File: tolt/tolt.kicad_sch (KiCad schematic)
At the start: 9 parts, among them J2 USB_C_Receptacle_USB2.0

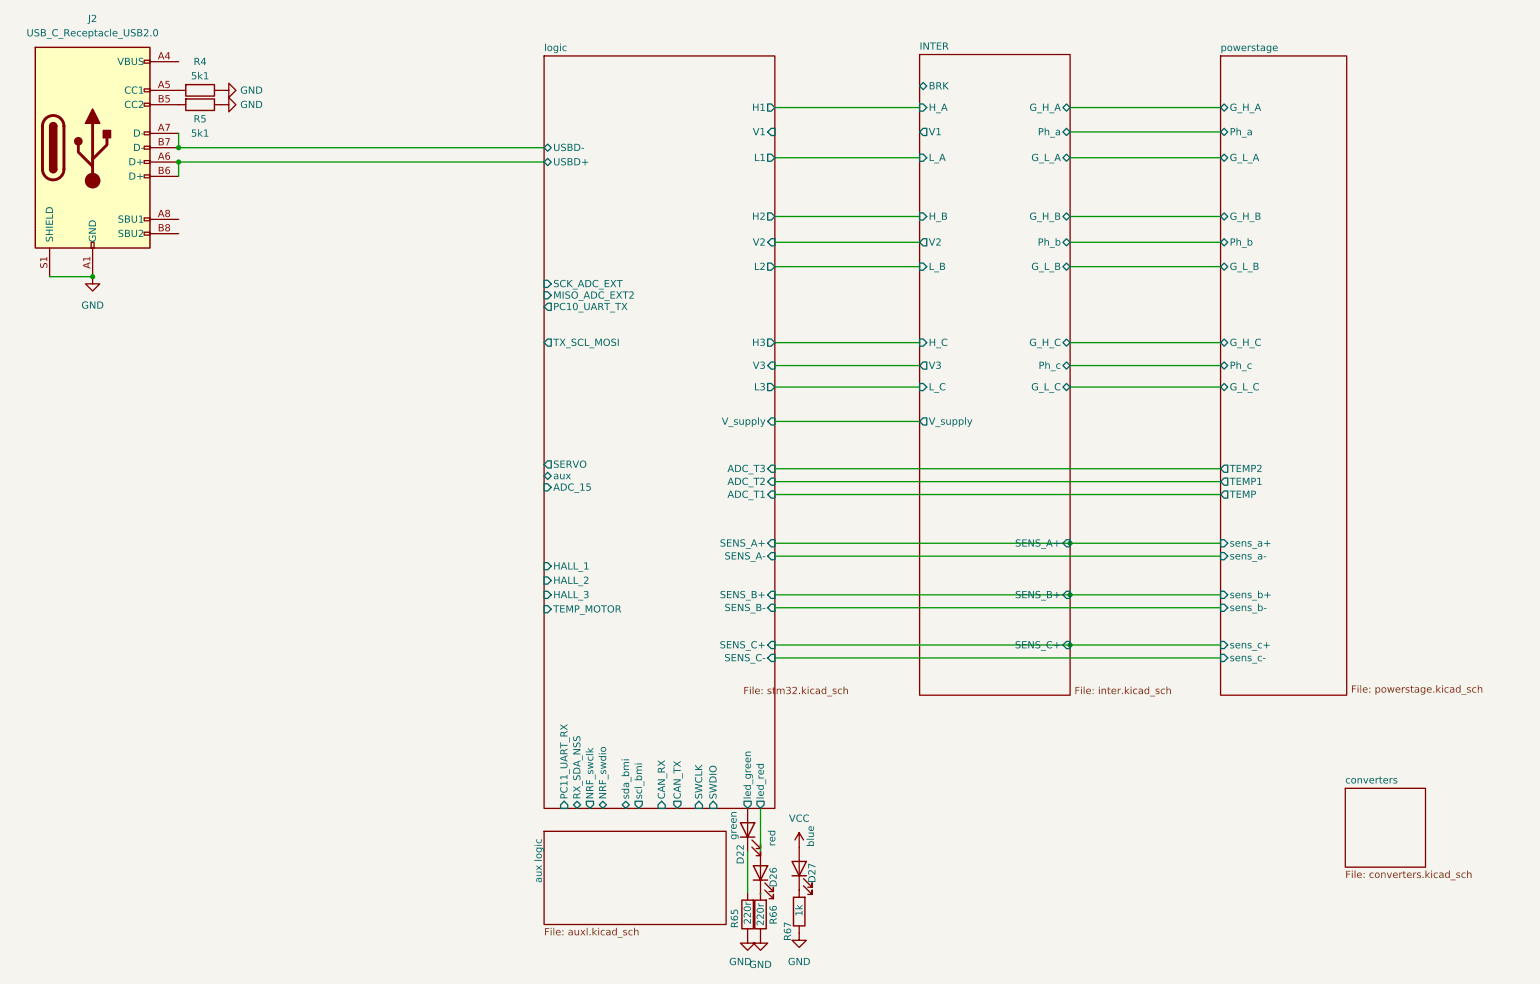
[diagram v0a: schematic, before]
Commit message: modified:   tolt/auxl.kicad_sch 	modified:   tolt/converters.kicad_sch 	modified:   tolt/powerstage.kicad_sch 	modified:   tolt/stm32.kicad_sch 	modified:   tolt/tolt.kicad_pcb 	modified:   tolt/tolt.kicad_pro 	modified:   tolt/tolt.kicad_sch 	SOP120P1500X235-17N.step 	tolt/Library.pretty/HDSOP-16-2.kicad_mod 	tolt/Library.pretty/R5930.kicad_mod 	tolt/conn.kicad_sch
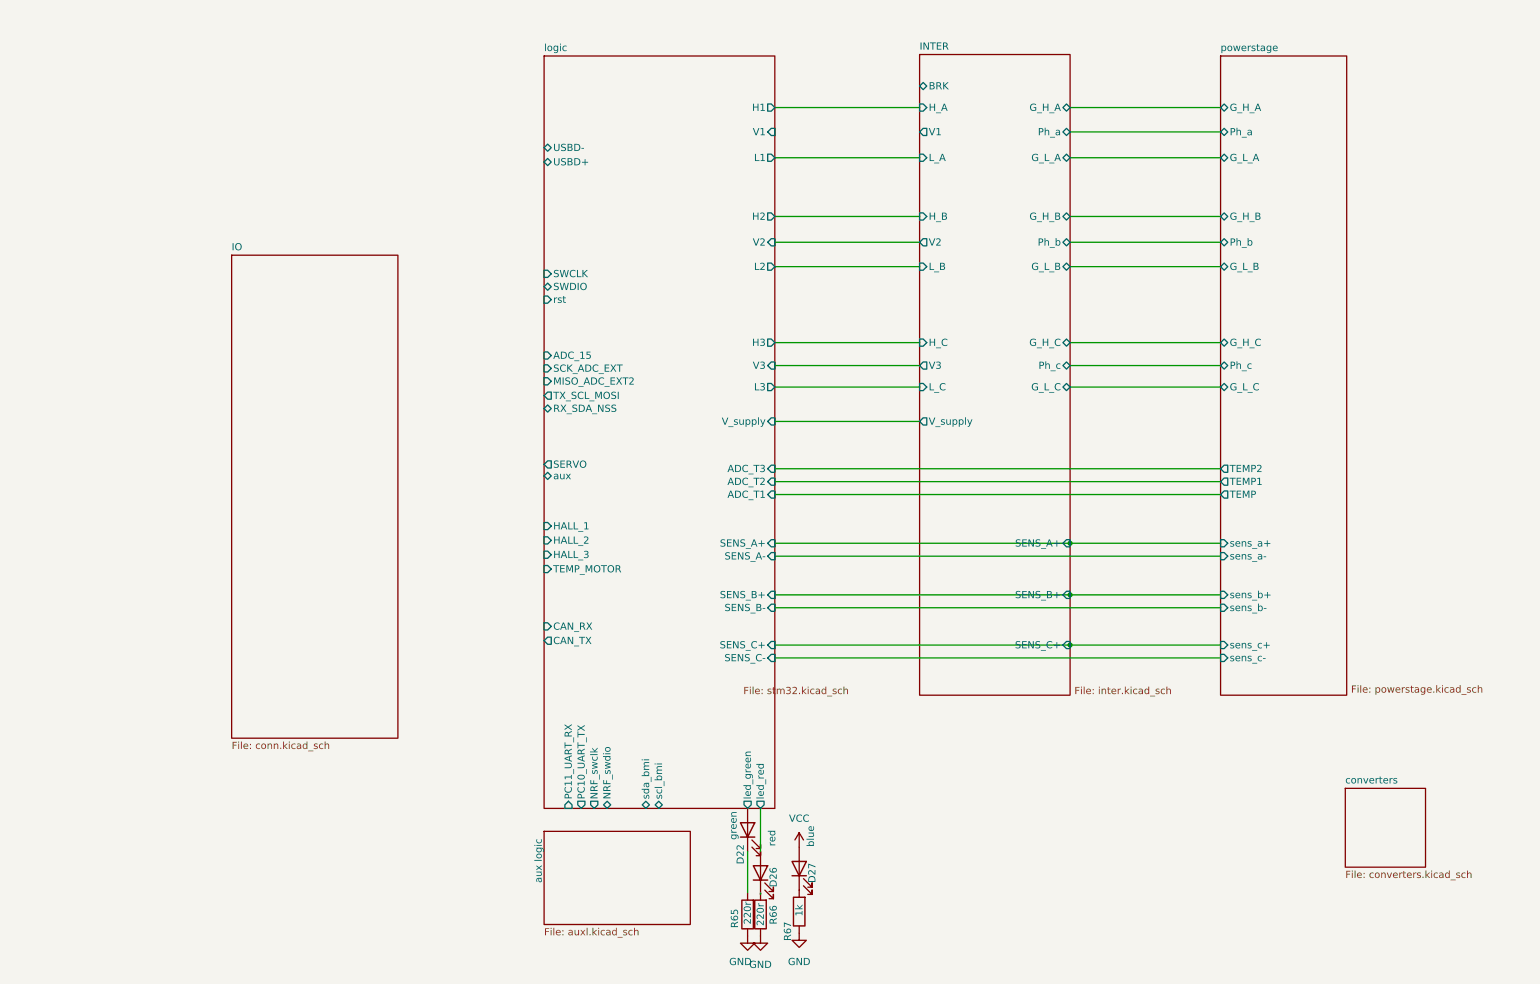
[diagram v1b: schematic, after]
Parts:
- removed J2: USB_C_Receptacle_USB2.0, Connector_USB:USB_C_Receptacle_G-Switch_GT-USB-7051x, symbol Connector:USB_C_Receptacle_USB2.0
- removed R4, R5: 5k1, Resistor_SMD:R_0603_1608Metric, symbol Device:R
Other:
- added sheet IO (conn.kicad_sch)
- sheet logic ports: added rst; removed none

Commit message: new file:   tolt/Library.pretty/IND-SMD_L3.9-W3.9-1.kicad_mod 	new file:   tolt/Library.pretty/IND-SMD_L5.0-W5.0.kicad_mod 	modified:   tolt/auxl.kicad_sch 	modified:   tolt/conn.kicad_sch 	modified:   tolt/converters.kicad_sch 	new file:   tolt/fp-lib-table 	modified:   tolt/inter.kicad_sch 	modified:   tolt/powerstage.kicad_sch 	modified:   tolt/stm32.kicad_sch 	modified:   tolt/tolt.kicad_sch
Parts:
- D22, D26, D27: footprint (none) -> Diode_SMD:D_0603_1608Metric_Pad1.05x0.95mm_HandSolder
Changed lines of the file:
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@@
 			)
 		)
-		(property "Footprint" ""
+		(property "Footprint" "Diode_SMD:D_0603_1608Metric_Pad1.05x0.95mm_HandSolder"
 			(at 146.812 165.354 0)
 			(effects
@@
 			)
 		)
-		(property "Footprint" ""
+		(property "Footprint" "Diode_SMD:D_0603_1608Metric_Pad1.05x0.95mm_HandSolder"
 			(at 153.67 164.592 0)
 			(effects
@@
 			)
 		)
-		(property "Footprint" ""
+		(property "Footprint" "Diode_SMD:D_0603_1608Metric_Pad1.05x0.95mm_HandSolder"
 			(at 144.526 157.734 0)
 			(effects
@@
 		)
 		(property "Sheetfile" "stm32.kicad_sch"
-			(at 143.764 132.334 0)
+			(at 153.67 150.876 0)
 			(effects
 				(font
@@
 	)
 	(sheet
-		(at 53.086 55.88)
-		(size 29.464 85.598)
+		(at 66.294 27.686)
+		(size 29.464 108.204)
 		(exclude_from_sim no)
 		(in_bom yes)
@@
 		)
 		(property "Sheetname" "IO"
-			(at 53.086 55.1684 0)
+			(at 66.294 26.9744 0)
 			(effects
 				(font
@@
 		)
 		(property "Sheetfile" "conn.kicad_sch"
-			(at 53.086 142.0626 0)
-			(effects
-				(font
+			(at 66.294 136.4746 0)
+			(effects
+				(font

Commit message: modified:   tolt/converters.kicad_sch 	modified:   tolt/inter.kicad_sch 	modified:   tolt/tolt.kicad_sch
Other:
- sheet IO ports: added ADC_15, CAN_RX, CAN_TX, HALL_1, HALL_2, HALL_3, MISO_ADC_EXT2, RX_SDA_NSS, SCK_ADC_EXT, SWCLK, SWDIO, TEMP_MOTOR, TX_SCL_MOSI, USBD+, USBD-, rst; removed none
- sheet aux logic ports: added PC10_UART_TX, PC11_UART_RX, scl_bmi, sda_bmi; removed none
